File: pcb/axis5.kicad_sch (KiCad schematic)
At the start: 10 parts, among them J15 Mini v1.0 FEMALE sockets, J25 MOTOR PHASES male 1x3, J35 ENCODER JST-SH 6p, J45 MINI POWER: +12V / GND

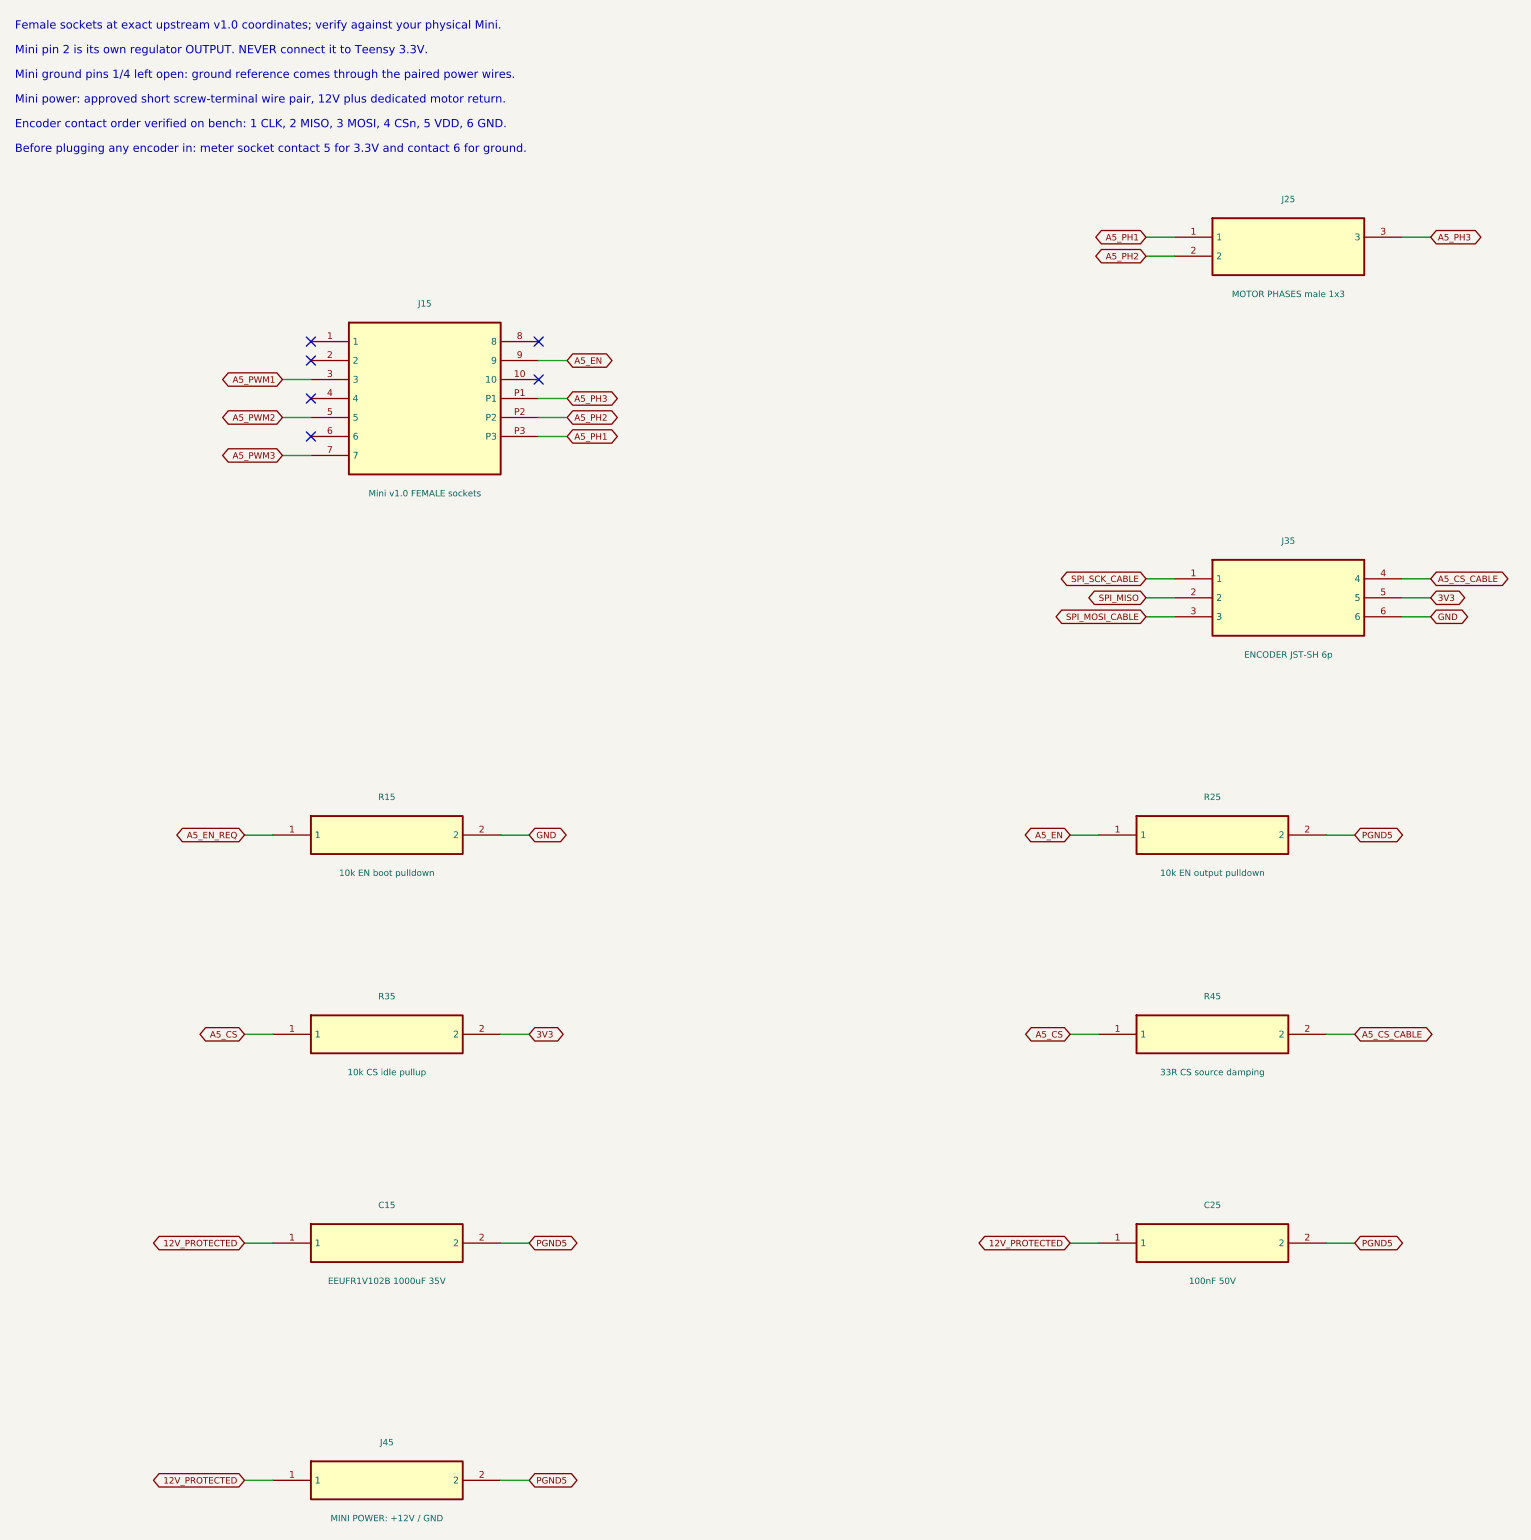
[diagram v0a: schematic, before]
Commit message: feat: finish through-hole six-axis carrier review design
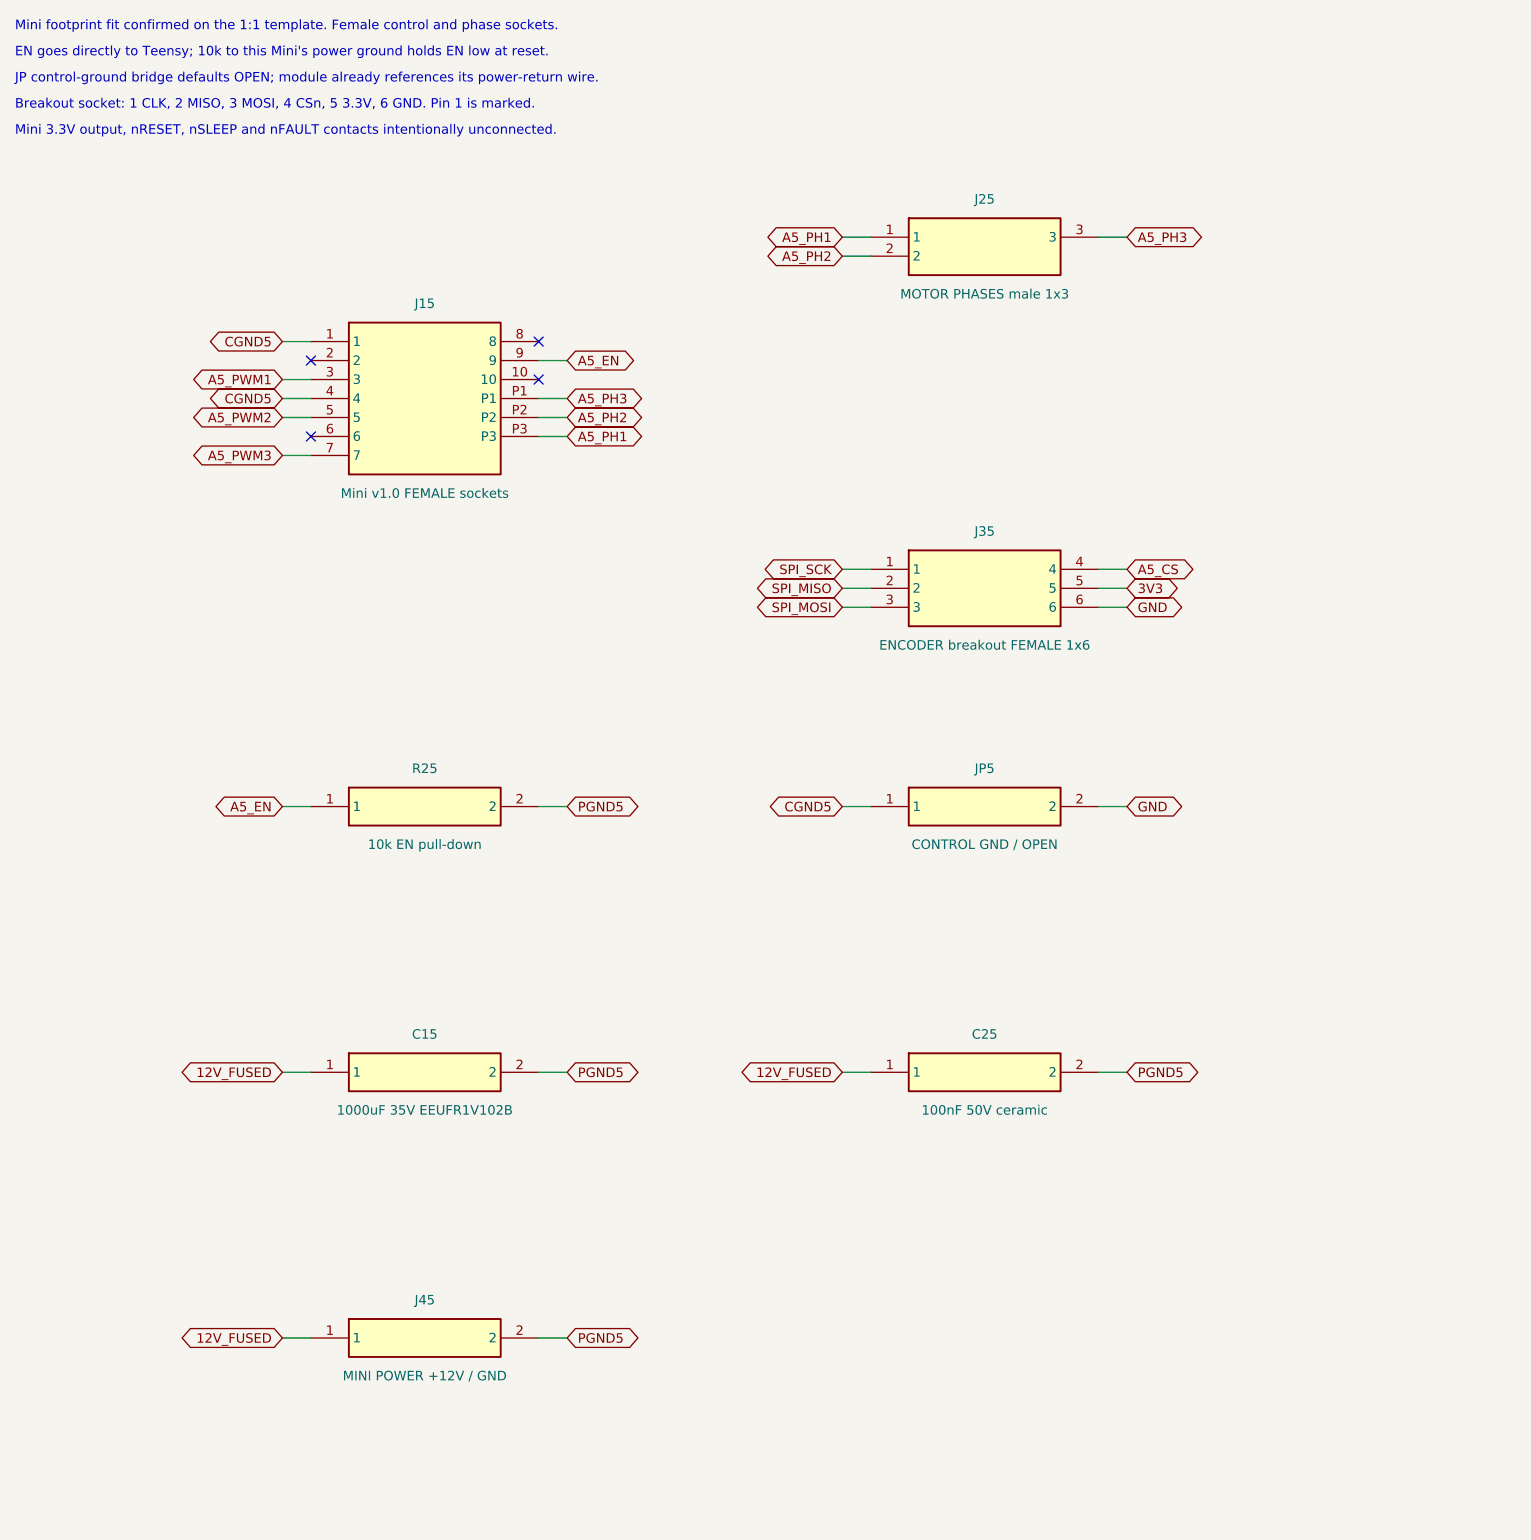
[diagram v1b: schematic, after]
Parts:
- removed R15: 10k EN boot pulldown, Resistor_SMD:R_0603_1608Metric, symbol TrueSkate:R15
- removed R35: 10k CS idle pullup, Resistor_SMD:R_0603_1608Metric, symbol TrueSkate:R35
- removed R45: 33R CS source damping, Resistor_SMD:R_0603_1608Metric, symbol TrueSkate:R45
- added JP5: CONTROL GND / OPEN, TrueSkate:GroundBridge_THT, symbol TrueSkate:JP5
- C15: value EEUFR1V102B 1000uF 35V -> 1000uF 35V EEUFR1V102B; LCSC C128476 -> (none)
- C25: value 100nF 50V -> 100nF 50V ceramic; footprint Capacitor_SMD:C_0603_1608Metric -> Capacitor_THT:C_Disc_D5.0mm_W2.5mm_P5.00mm; LCSC C14663 -> (none)
- J35: value ENCODER JST-SH 6p -> ENCODER breakout FEMALE 1x6; footprint Connector_JST:JST_SH_BM06B-SRSS-TB_1x06-1MP_P1.00mm_Vertical -> Connector_PinSocket_2.54mm:PinSocket_1x06_P2.54mm_Vertical; LCSC C160392 -> (none)
- J45: value MINI POWER: +12V / GND -> MINI POWER +12V / GND
- R25: value 10k EN output pulldown -> 10k EN pull-down; footprint Resistor_SMD:R_0603_1608Metric -> Resistor_THT:R_Axial_DIN0207_L6.3mm_D2.5mm_P7.62mm_Horizontal; LCSC C25804 -> (none)
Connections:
- net A5_CS_CABLE is gone; now on net A5_CS: J35.4
- net GND: now also JP5.2
- net CGND5: now reaches J15.1
- net CGND5: now also J15.4, JP5.1
- net 12V_PROTECTED renamed 12V_FUSED
- net SPI_MOSI_CABLE renamed SPI_MOSI
- net SPI_SCK_CABLE renamed SPI_SCK
- no-connect marks 6 -> 4
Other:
- note added: "Breakout socket: 1 CLK, 2 MISO, 3 MOSI, 4 CSn, 5 3.3V, 6 GND. Pin 1 is marked."
- note added: "EN goes directly to Teensy; 10k to this Mini's power ground holds EN low at reset."
- note added: "JP control-ground bridge defaults OPEN; module already references its power-return wire."
- note added: "Mini 3.3V output, nRESET, nSLEEP and nFAULT contacts intentionally unconnected."
- note added: "Mini footprint fit confirmed on the 1:1 template. Female control and phase sockets."
- note removed: "Before plugging any encoder in: meter socket contact 5 for 3.3V and contact 6 for ground."
- note removed: "Encoder contact order verified on bench: 1 CLK, 2 MISO, 3 MOSI, 4 CSn, 5 VDD, 6 GND."
- note removed: "Female sockets at exact upstream v1.0 coordinates; verify against your physical Mini."
- note removed: "Mini ground pins 1/4 left open: ground reference comes through the paired power wires."
- note removed: "Mini pin 2 is its own regulator OUTPUT. NEVER connect it to Teensy 3.3V."
- note removed: "Mini power: approved short screw-terminal wire pair, 12V plus dedicated motor return."
- title: 07 / Axis 5: middle_curl_2 -> 06 / A5: middle_curl_2
- moved on the sheet: C15, C25, J25, J35, J45, R25

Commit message: feat: use exact Mini v1.0 footprints with direct power routing
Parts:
- removed J45: MINI POWER +12V / GND, TerminalBlock_Phoenix:TerminalBlock_Phoenix_MKDS-1-2-3.81_1x02_P3.81mm_Horizontal, symbol TrueSkate:J45
- J15: value Mini v1.0 FEMALE sockets -> Mini v1.0 / 15-hole socket; footprint TrueSkate:Mini_v1_Sockets -> TrueSkate:SimpleFOC_Mini_v1.0
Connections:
- net 12V_FUSED: now also J15.VIN
- net PGND5: now also J15.GND
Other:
- note added: "JP control-ground bridge defaults OPEN; module references its directly routed power-return pad."
- note added: "Mini v1.0: exact 15-hole footprint; component side up, pins down; NOT mirrored."
- note removed: "JP control-ground bridge defaults OPEN; module already references its power-return wire."
- note removed: "Mini footprint fit confirmed on the 1:1 template. Female control and phase sockets."
